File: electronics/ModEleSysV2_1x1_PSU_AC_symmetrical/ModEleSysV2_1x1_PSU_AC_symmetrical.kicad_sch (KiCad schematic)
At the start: 29 parts, among them J2 Jack-DC, SW1 switch_DPDT, U1 LM317, U2 LM337

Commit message: WIP placement of parts and reducing sizes, it is a bit cramped
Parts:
- R1, R2, R3, R4, R5, R6: footprint SquantorResistor:R_0805+0603 -> SquantorResistor:R_0603_hand
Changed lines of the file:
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@@
       (effects (font (size 1.27 1.27)))
     )
-    (property "Footprint" "SquantorResistor:R_0805+0603" (at 132.08 38.608 90)
+    (property "Footprint" "SquantorResistor:R_0603_hand" (at 132.08 38.608 90)
       (effects (font (size 1.27 1.27)) hide)
     )
@@
       (effects (font (size 1.27 1.27)))
     )
-    (property "Footprint" "SquantorResistor:R_0805+0603" (at 95.25 38.608 90)
+    (property "Footprint" "SquantorResistor:R_0603_hand" (at 95.25 38.608 90)
       (effects (font (size 1.27 1.27)) hide)
     )
@@
       (effects (font (size 1.27 1.27)))
     )
-    (property "Footprint" "SquantorResistor:R_0805+0603" (at 132.08 43.688 90)
+    (property "Footprint" "SquantorResistor:R_0603_hand" (at 132.08 43.688 90)
       (effects (font (size 1.27 1.27)) hide)
     )
@@
       (effects (font (size 1.27 1.27)))
     )
-    (property "Footprint" "SquantorResistor:R_0805+0603" (at 132.08 41.148 90)
+    (property "Footprint" "SquantorResistor:R_0603_hand" (at 132.08 41.148 90)
       (effects (font (size 1.27 1.27)) hide)
     )
@@
       (effects (font (size 1.27 1.27)))
     )
-    (property "Footprint" "SquantorResistor:R_0805+0603" (at 95.25 43.688 90)
+    (property "Footprint" "SquantorResistor:R_0603_hand" (at 95.25 43.688 90)
       (effects (font (size 1.27 1.27)) hide)
     )
@@
       (effects (font (size 1.27 1.27)))
     )
-    (property "Footprint" "SquantorResistor:R_0805+0603" (at 95.25 41.148 90)
-      (effects (font (size 1.27 1.27)) hide)
-    )
+    (property "Footprint" "SquantorResistor:R_0603_hand" (at 95.25 41.148 90)
+      (effects (font (size 1.27 1.27)) hide)
+    )

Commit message: done, needs review in between
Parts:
- added C9: 10n, SquantorCapacitor:C_0805+0603, symbol Device:C
- D1, D2: value D -> A7
- D3, D5: value D -> B5819WS; footprint SquantorDiodes:SOD-123F-hand -> SquantorDiodes:SOD-323HE-shikues
- D4, D6: value D -> B5819WS; footprint SquantorDiodes:SOD-323-nexperia-hand -> SquantorDiodes:SOD-323HE-shikues
- F1: value Fuse -> 0.6A 60V
- N1: value 20240311 -> 20240329
- R1, R2, R4, R5: value R -> TBD
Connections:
- net AC1_PHASE: now also C9.1
- net GND: now also C9.2
- net +adj: now reaches C5.1, D4.2 (A), R1.1, R2.1, R3.1, U1.1 (ADJ)
- net -adj: now reaches C8.1, D6.1 (K), R4.1, R5.1, R6.1, U2.1 (ADJ)
- no-connect marks 23 -> 25

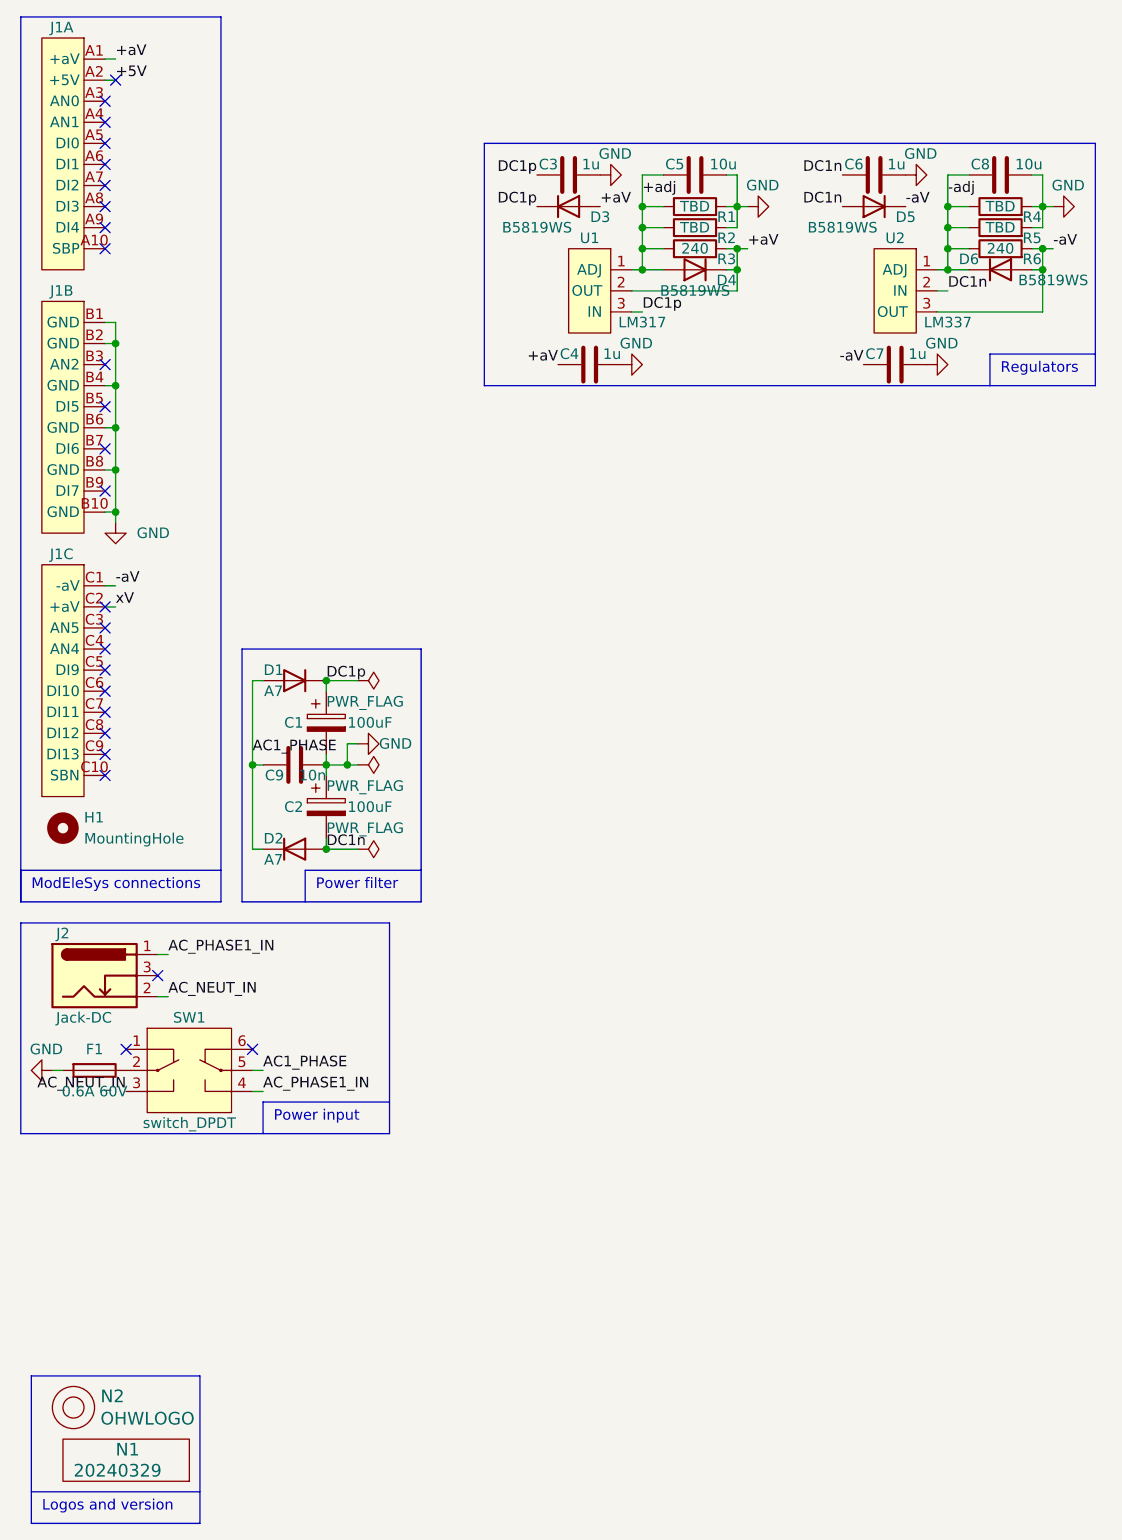
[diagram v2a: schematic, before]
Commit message: reviewed and different placement of switch and power input
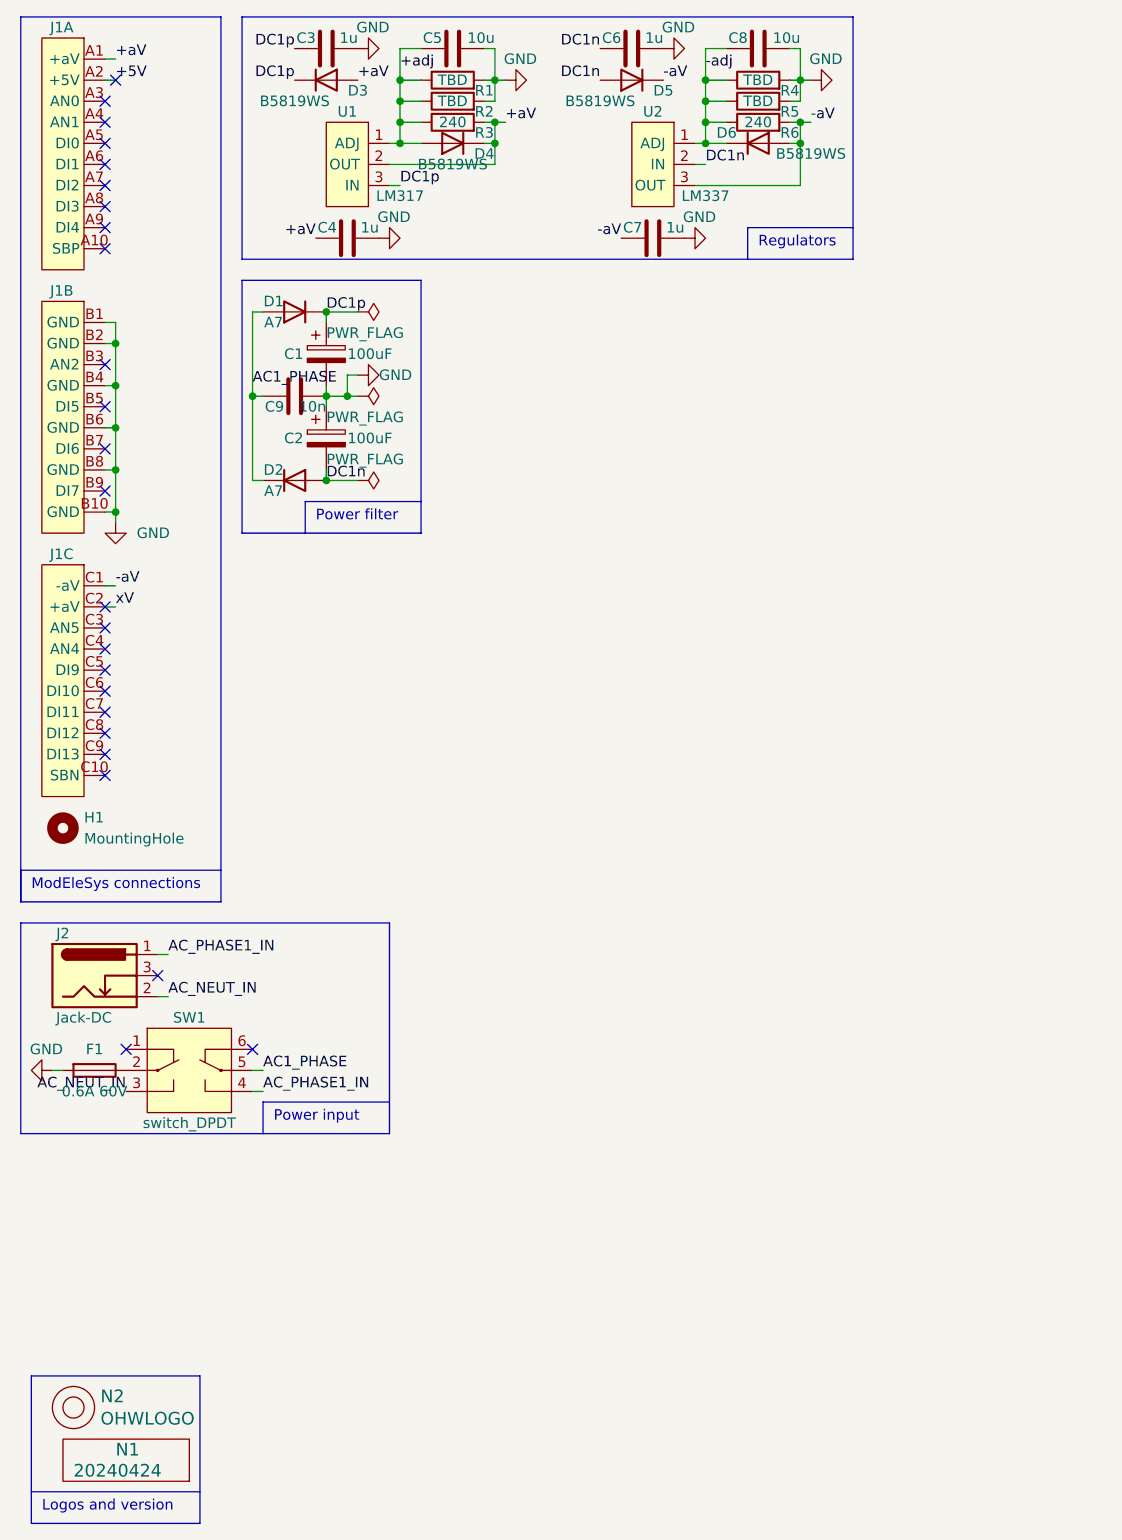
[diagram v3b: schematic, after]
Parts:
- C4, C7: footprint SquantorCapacitor:C_0805+0603 -> SquantorCapacitor:C_1206_0805
- N1: value 20240329 -> 20240424
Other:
- moved on the sheet: C1, C2, C3, C4, C5, C6, C7, C8, C9, D1, D2, D3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

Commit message: updated versionnumbers
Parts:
- N1: value 20240424 -> 20240426
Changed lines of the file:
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@@
       (effects (font (size 1.524 1.524)) (justify left))
     )
-    (property "Value" "20240424" (at 20.32 189.23 0)
+    (property "Value" "20240426" (at 20.32 189.23 0)
       (effects (font (size 1.524 1.524)) (justify left))
     )

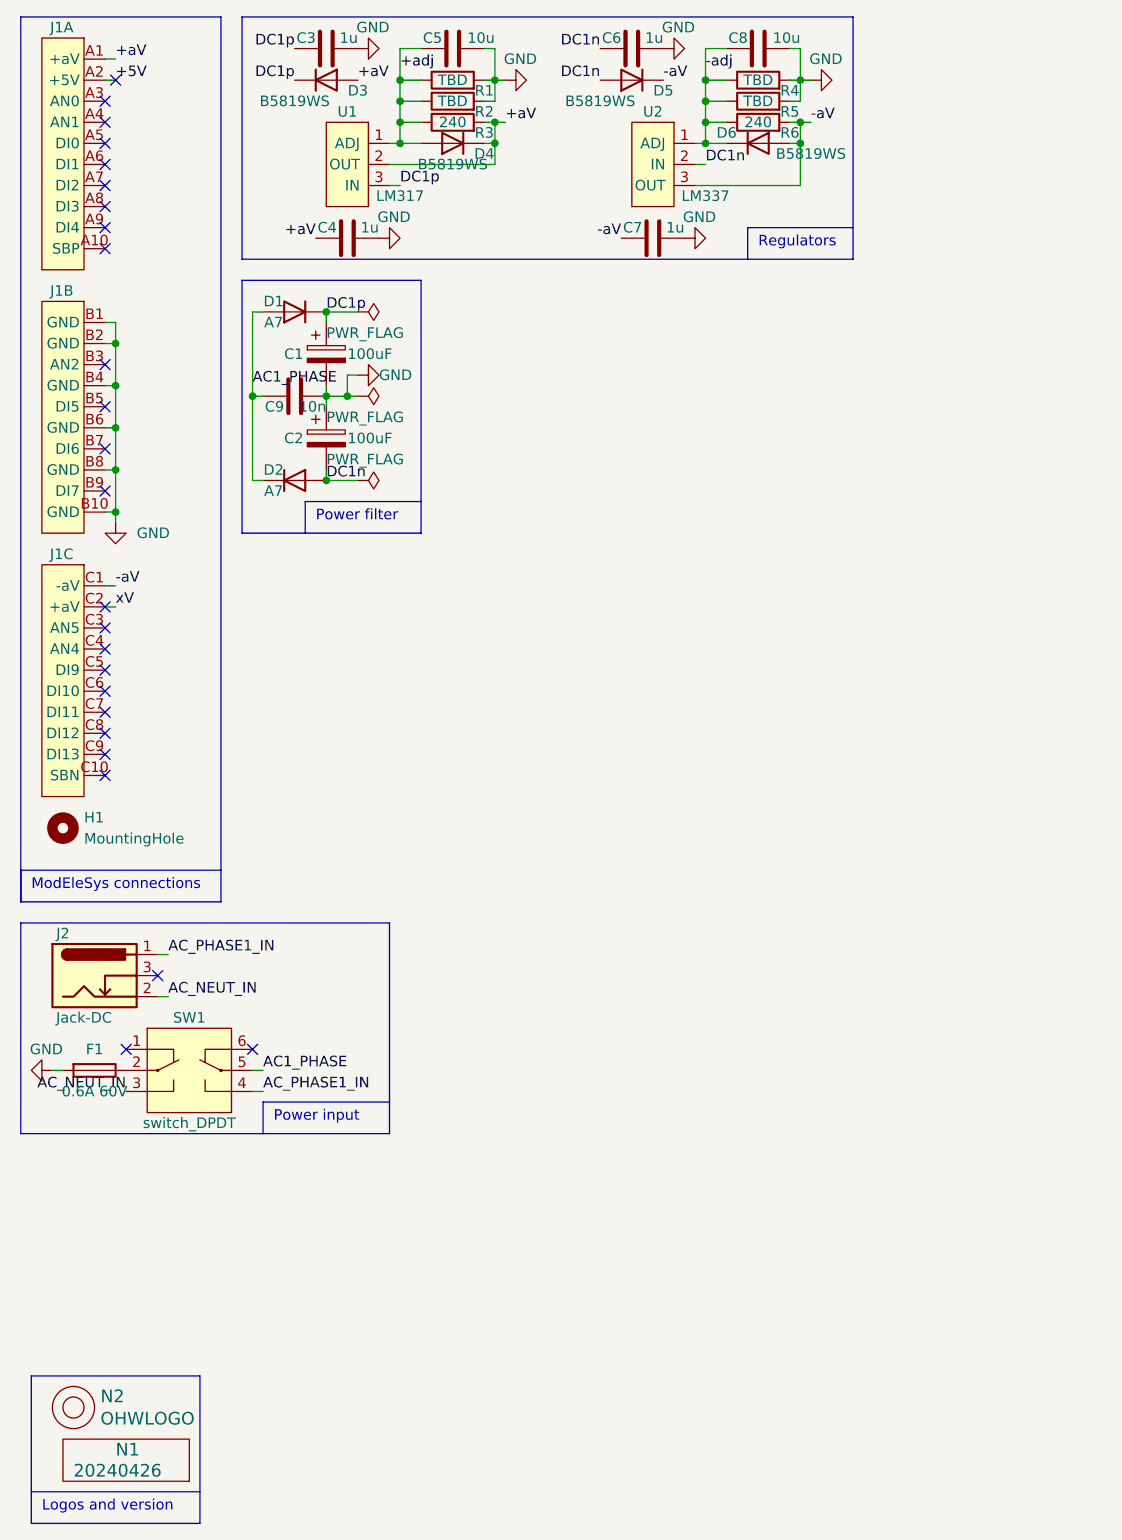
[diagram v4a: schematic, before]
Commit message: updated PCB with easier to place components and added more output capacitance
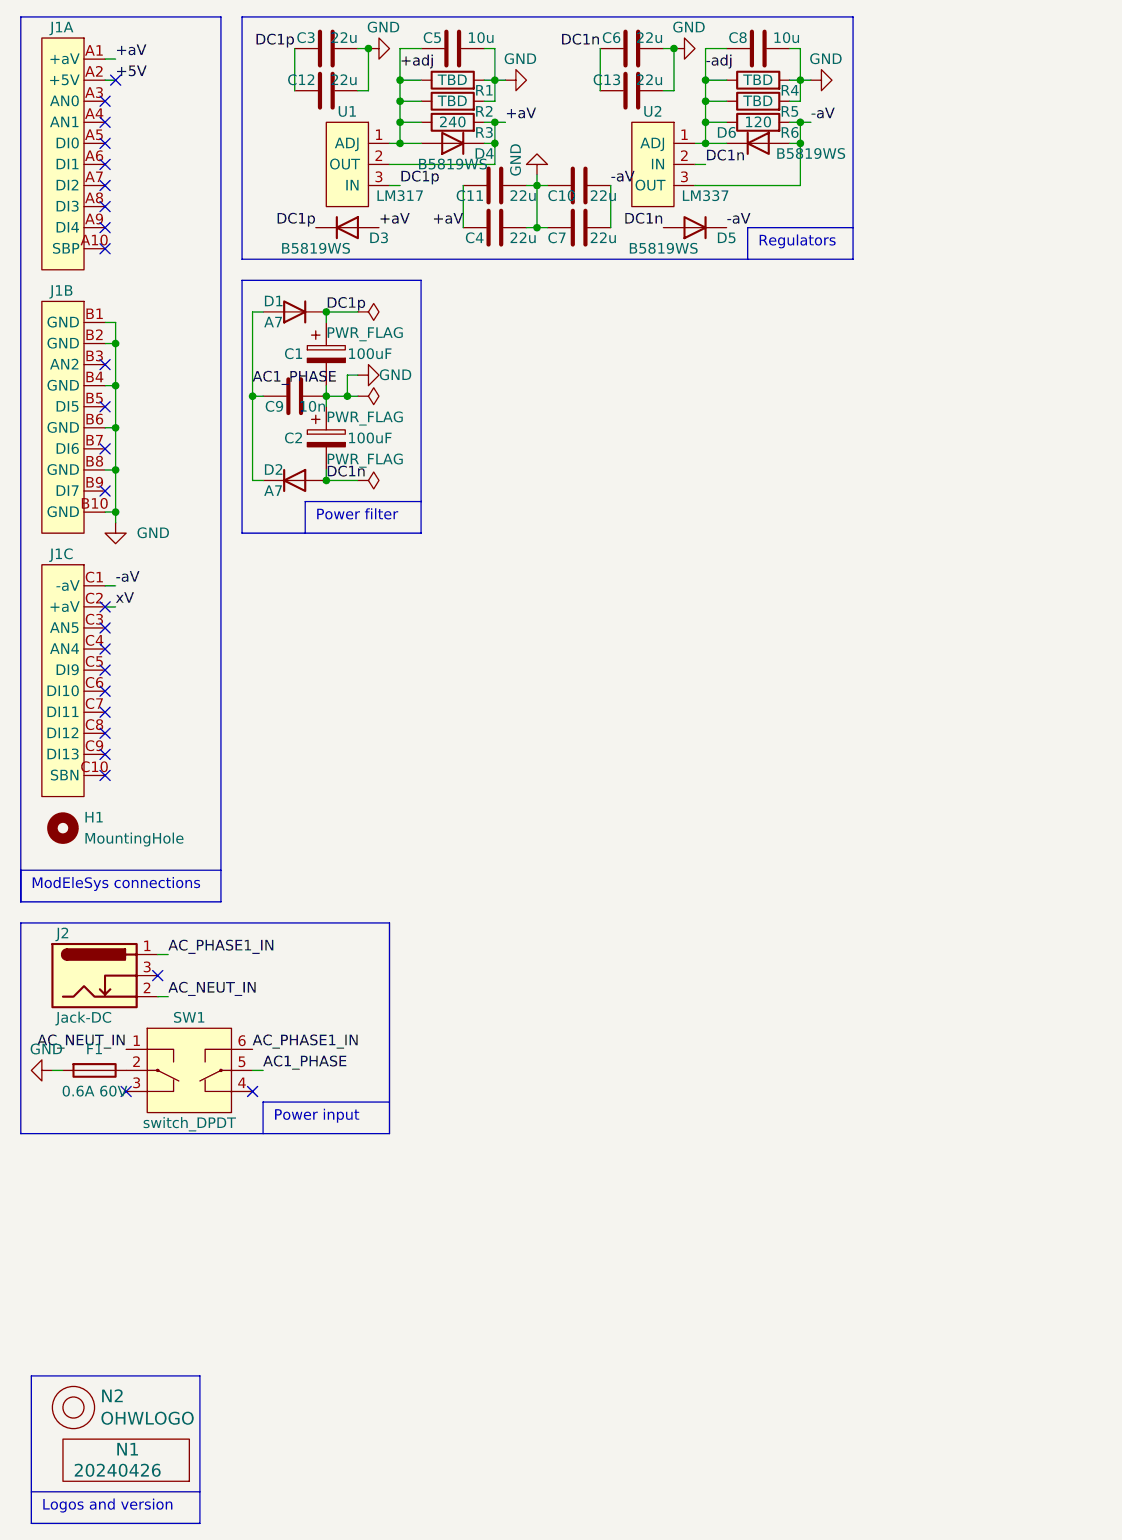
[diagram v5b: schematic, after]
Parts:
- added C10, C11, C12, C13: 22u, SquantorCapacitor:C_1206_0805, symbol Device:C
- C3, C6: value 1u -> 22u; footprint SquantorCapacitor:C_0805+0603 -> SquantorCapacitor:C_1206_0805
- C4, C7: value 1u -> 22u
- D3, D4, D5, D6: footprint SquantorDiodes:SOD-323HE-shikues -> SquantorDiodes:SOD-323-nexperia-hand
- R1, R2, R3, R4, R5: footprint SquantorResistor:R_0603_hand -> SquantorResistor:R_0805+0603
- R6: value 240 -> 120; footprint SquantorResistor:R_0603_hand -> SquantorResistor:R_0805+0603
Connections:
- net +aV: now also C11.1
- net -aV: now also C10.1
- net AC_NEUT_IN: now also SW1.1 (SW1_P1); no longer SW1.3 (SW1_P2)
- net AC_PHASE1_IN: now also SW1.6 (SW2_P2); no longer SW1.4 (SW2_P2)
- net DC1n: now also C13.1
- net DC1p: now also C12.1
- net GND: now also C10.2, C11.2, C12.2, C13.2
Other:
- moved on the sheet: C4, C7, D3, D5

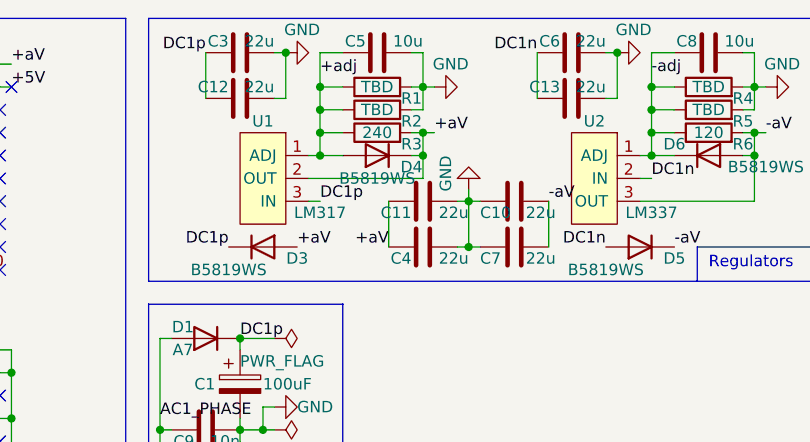
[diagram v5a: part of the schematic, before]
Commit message: some more PCB modifications, changing output caps to larger values
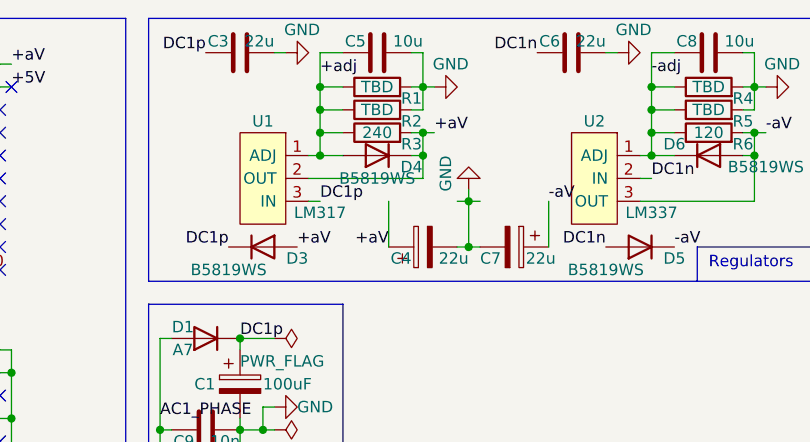
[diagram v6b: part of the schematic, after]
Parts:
- removed C10, C11, C12, C13: 22u, SquantorCapacitor:C_1206_0805, symbol Device:C
- C4, C7: footprint SquantorCapacitor:C_1206_0805 -> SquantorCapacitor:C-025-065-elco; symbol Device:C -> Device:C_Polarized
